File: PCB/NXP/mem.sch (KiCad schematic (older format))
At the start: 14 parts, among them U12 24AA1025, U13 24AA025E48, U20 S25FL032P0XMFI013

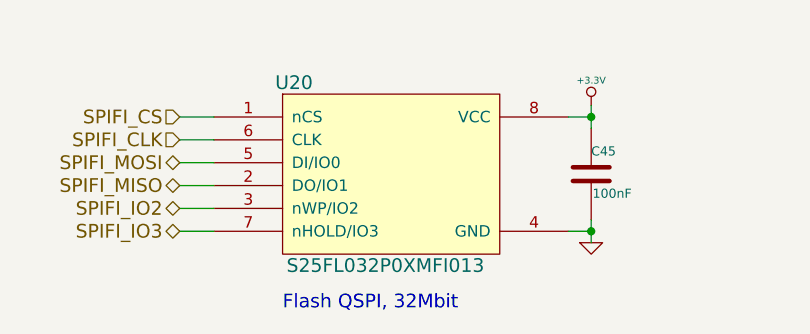
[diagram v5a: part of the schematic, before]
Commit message: #54 CIAA-NXP flash qSPI memory part updated in schematic and BOM. No need to change PCB.
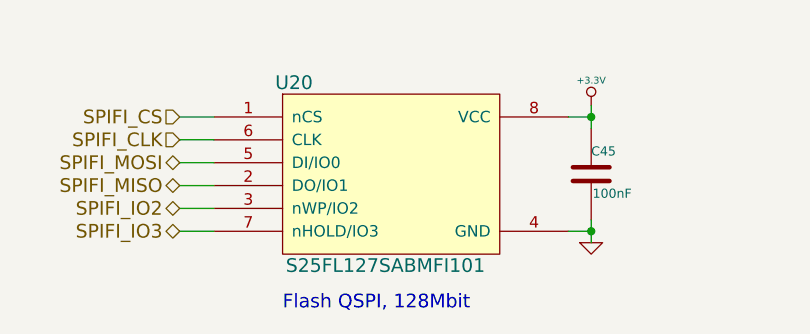
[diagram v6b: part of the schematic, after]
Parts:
- U20: value S25FL032P0XMFI013 -> S25FL127SABMFI101
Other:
- note added: "Flash QSPI, 128Mbit"
- note removed: "Flash QSPI, 32Mbit"
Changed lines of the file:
@@
 Sheet 11 12
 Title "CIAA micro SD card"
-Date "25 mar 2015"
+Date "11 may 2015"
 Rev "1.0"
 Comp ""
@@
 P 5450 4250
 F 0 "U20" H 5050 4650 60  0000 C CNN
-F 1 "S25FL032P0XMFI013" H 5450 3850 60  0000 C CNN
+F 1 "S25FL127SABMFI101" H 5450 3850 60  0000 C CNN
 F 2 "~" H 5450 4050 60  0000 C CNN
 F 3 "~" H 5450 4050 60  0000 C CNN
@@
 EEPROM, 2kbit, EUI-48 Node Identity
 Text Notes 5000 4850 0    60   ~ 0
-Flash QSPI, 32Mbit
+Flash QSPI, 128Mbit
 $EndSCHEMATC

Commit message: [ciaa-nxp] schematic layout fixed for newer versions of kicad
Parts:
- C19, C20, C45: symbol C -> C-RESCUE-ciaa-nxp
- R23, R24, R25, R26, R27, R28, R29, R30: symbol R -> R-RESCUE-ciaa-nxp
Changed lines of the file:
@@
 EESchema Schematic File Version 2
+LIBS:ciaa-nxp-rescue
 LIBS:power
 LIBS:device
@@
 LIBS:memory
 LIBS:xilinx
-LIBS:special
 LIBS:microcontrollers
 LIBS:dsp
@@
 LIBS:fqt13n06l
 LIBS:ciaa-nxp-cache
-EELAYER 27 0
+EELAYER 25 0
 EELAYER END
 $Descr A4 11693 8268
@@
 	5150 2300 5000 2300
 $Comp
-L GND #PWR0225
+L GND-RESCUE-ciaa-nxp #PWR0225
 U 1 1 52E536B1
 P 4300 2600
@@
 $EndComp
 $Comp
-L +3.3V #PWR0226
+L +3.3V-RESCUE-ciaa-nxp #PWR0226
 U 1 1 52E536B7
 P 4300 1150
@@
 	4300 2600 4300 2600
 $Comp
-L C C19
+L C-RESCUE-ciaa-nxp C19
 U 1 1 52E536BF
 P 4650 1400
@@
 $EndComp
 $Comp
-L GND #PWR0227
+L GND-RESCUE-ciaa-nxp #PWR0227
 U 1 1 52E536C5
 P 3350 2600
@@
 $EndComp
 $Comp
-L GND #PWR0228
+L GND-RESCUE-ciaa-nxp #PWR0228
 U 1 1 52E536CB
 P 3200 2600
@@
 $EndComp
 $Comp
-L GND #PWR0229
+L GND-RESCUE-ciaa-nxp #PWR0229
 U 1 1 52E536D1
 P 4650 1650
@@
 	5000 2000 5150 2000
 $Comp
-L GND #PWR0230
+L GND-RESCUE-ciaa-nxp #PWR0230
 U 1 1 52E536DF
 P 5350 1550
@@
 Connection ~ 4300 1200
 $Comp
-L +3.3V #PWR0231
+L +3.3V-RESCUE-ciaa-nxp #PWR0231
 U 1 1 52E536E8
 P 3500 2600
@@
 	7850 2300 8500 2300
 $Comp
-L GND #PWR0232
+L GND-RESCUE-ciaa-nxp #PWR0232
 U 1 1 52E536F8
 P 7150 2600
@@
 $EndComp
 $Comp
-L +3.3V #PWR0233
+L +3.3V-RESCUE-ciaa-nxp #PWR0233
 U 1 1 52E536FE
 P 7150 1150
@@
 	7150 2600 7150 2600
 $Comp
-L C C20
+L C-RESCUE-ciaa-nxp C20
 U 1 1 52E53706
 P 7500 1400
@@
 $EndComp
 $Comp
-L GND #PWR0234
+L GND-RESCUE-ciaa-nxp #PWR0234
 U 1 1 52E5370C
 P 6200 2600
@@
 $EndComp
 $Comp
-L GND #PWR0235
+L GND-RESCUE-ciaa-nxp #PWR0235
 U 1 1 52E53712
 P 7500 1650
@@
 	7850 2000 8000 2000
 $Comp
-L GND #PWR0236
+L GND-RESCUE-ciaa-nxp #PWR0236
 U 1 1 52E5371B
 P 8200 1550
@@
 Connection ~ 7150 1200
 $Comp
-L +3.3V #PWR0237
+L +3.3V-RESCUE-ciaa-nxp #PWR0237
 U 1 1 52E53724
 P 6050 2600
@@
 $EndComp
 $Comp
-L GND #PWR0238
+L GND-RESCUE-ciaa-nxp #PWR0238
 U 1 1 52E5372A
 P 6350 2600
@@
 $EndComp
 $Comp
-L R R25
+L R-RESCUE-ciaa-nxp R25
 U 1 1 52E53730
 P 3200 2350
@@
 $EndComp
 $Comp
-L R R26
+L R-RESCUE-ciaa-nxp R26
 U 1 1 52E53736
 P 3350 2350
@@
 $EndComp
 $Comp
-L R R27
+L R-RESCUE-ciaa-nxp R27
 U 1 1 52E5373C
 P 3500 2350
@@
 $EndComp
 $Comp
-L R R23
+L R-RESCUE-ciaa-nxp R23
 U 1 1 52E53742
 P 5150 1750
@@
 	6350 2100 6450 2100
 $Comp
-L R R28
+L R-RESCUE-ciaa-nxp R28
 U 1 1 52E5374D
 P 6050 2350
@@
 $EndComp
 $Comp
-L R R29
+L R-RESCUE-ciaa-nxp R29
 U 1 1 52E53753
 P 6200 2350
@@
 $EndComp
 $Comp
-L R R30
+L R-RESCUE-ciaa-nxp R30
 U 1 1 52E53759
 P 6350 2350
@@
 $EndComp
 $Comp
-L R R24
+L R-RESCUE-ciaa-nxp R24
 U 1 1 52E5375F
 P 8000 1750
@@
 $EndComp
 $Comp
-L C C45
+L C-RESCUE-ciaa-nxp C45
 U 1 1 52E54038
 P 6350 4250
@@
 	6350 4450 6350 4550
 $Comp
-L +3.3V #PWR0239
+L +3.3V-RESCUE-ciaa-nxp #PWR0239
 U 1 1 52E5407E
 P 6350 3950
@@
 Connection ~ 6350 4000
 $Comp
-L GND #PWR0240
+L GND-RESCUE-ciaa-nxp #PWR0240
 U 1 1 52E540A7
 P 6350 4550
